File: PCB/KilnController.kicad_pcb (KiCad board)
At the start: 2 copper layers, 150 x 85 mm, 30 parts, among them J1 12V 3A PS Header, J10 Display Header, J11 Display Button Header, J12 Moisture Probe 1 Header, J13 Moisture Probe 2 Header, J2 Exhaust Fan Header, J3 Circulation Fan Header, J4 SD Card Module, J5 Exhaust Servo Header, J6 Intake Servo Header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

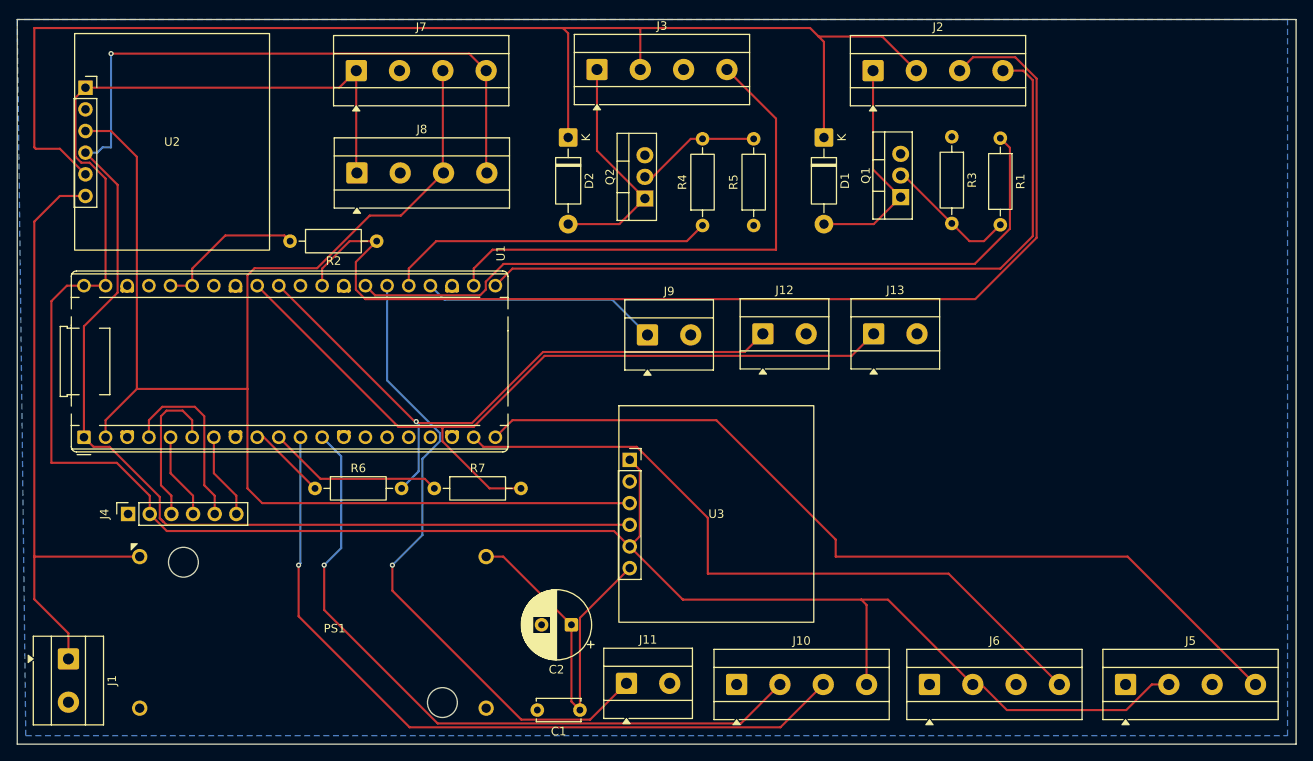
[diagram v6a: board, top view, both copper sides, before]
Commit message: Add LoRa to schematic & layout
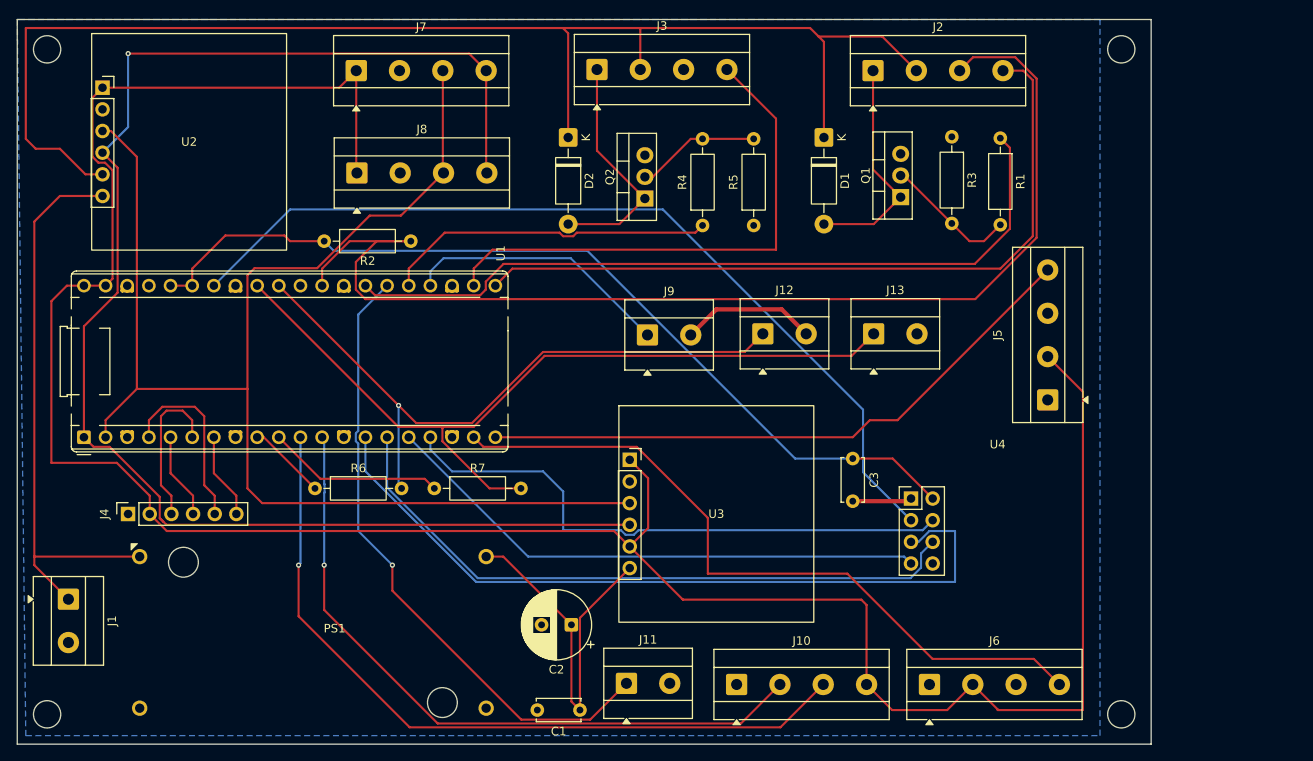
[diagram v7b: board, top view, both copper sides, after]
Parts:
- added C3: 100nF, Capacitor_THT:C_Disc_D5.0mm_W2.5mm_P5.00mm, F.Cu at (177.0, 110.5)
- added REF**: MountingHole_3.2mm_M3, MountingHole:MountingHole_3.2mm_M3, F.Cu at (82.5, 140.5)
- added REF**: MountingHole_3.2mm_M3, MountingHole:MountingHole_3.2mm_M3, F.Cu at (208.5, 62.5)
- added REF**: MountingHole_3.2mm_M3, MountingHole:MountingHole_3.2mm_M3, F.Cu at (208.5, 140.5)
- added REF**: MountingHole_3.2mm_M3, MountingHole:MountingHole_3.2mm_M3, F.Cu at (82.5, 62.5)
- added U4: Ra-02_433MHz, KilnFootprintLibrary:LoRa_Module, F.Cu at (183.8, 115.2)
- J4: footprint Connector_PinSocket_2.54mm:PinSocket_1x06_P2.54mm_Vertical -> KilnFootprintLibrary:SDCardModule
- moved J5 34.6 mm to (199.9, 103.6), turned to 90 degrees
- moved J1 7.00 mm to (85.0, 127.0)
- moved R2 4.00 mm to (115.0, 85.0)
- moved U2 2.00 mm to (89.0, 67.0)
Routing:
- net /LORA_RST: track 0.00 -> 104.9 mm
- net /LORA_SCK: track 0.00 -> 91.0 mm
- net /+3V3: track 17.9 -> 105.8 mm
- net /LORA_TX: track 0.00 -> 77.0 mm
- net /LORA_CS: track 0.00 -> 67.9 mm
- net /LORA_RX: track 0.00 -> 65.0 mm
- net /SERVO_EXHAUST: track 104.0 -> 72.9 mm
- net /+5V: track 263.4 -> 292.5 mm
- net GND: track 0.00 -> 22.9 mm
- net /FAN_EX_TACH: track 129.1 -> 137.1 mm
- net /+12V_SRC: track 72.6 -> 67.6 mm
- net /I2C0_SDA: track 178.0 -> 173.8 mm
- net /HEATER_SSR: track 27.9 -> 31.5 mm
- net /+12V: track 156.9 -> 160.3 mm
- net /I2C0_SCL: track 165.2 -> 163.2 mm
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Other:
- board size 150 x 85 mm -> 133 x 85 mm

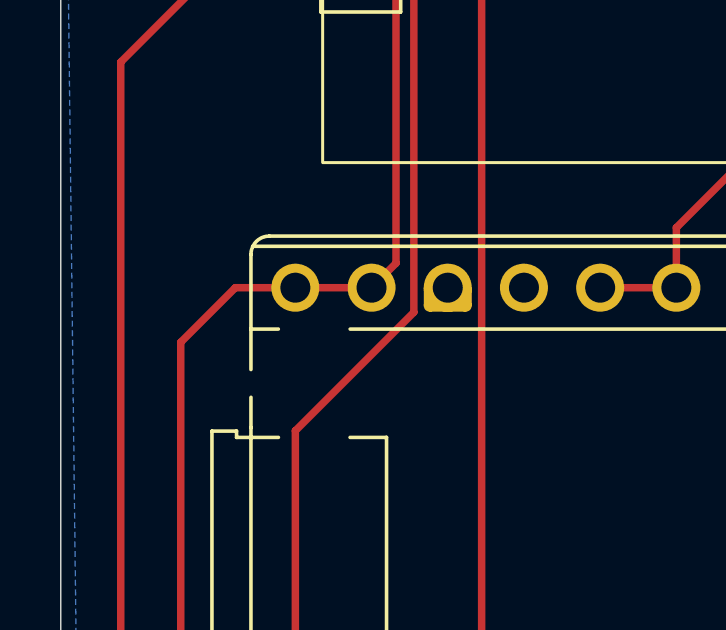
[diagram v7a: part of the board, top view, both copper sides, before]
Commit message: Remove VBUS connection
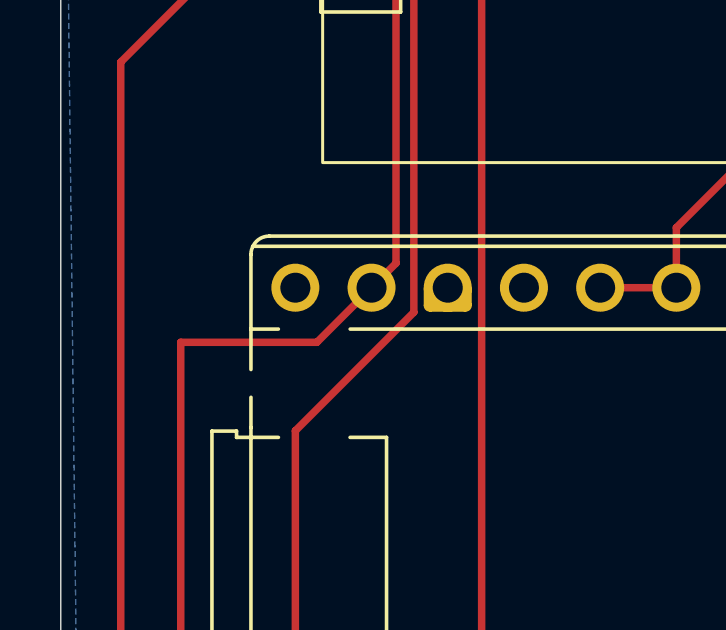
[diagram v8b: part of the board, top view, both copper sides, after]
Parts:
- J4: footprint KilnFootprintLibrary:SDCardModule -> Connector_PinSocket_2.54mm:PinSocket_1x06_P2.54mm_Vertical
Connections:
- U1 pad 40: /+5V -> unconnected-(U1-VBUS-Pad40)
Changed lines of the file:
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@@
 	(net 41 "/I2C0_SDA")
 	(net 42 "unconnected-(U4-DIO0-Pad8)")
+	(net 43 "unconnected-(U1-VBUS-Pad40)")
 	(footprint "KilnFootprintLibrary:TerminalBlock_MetzConnect_Type101_RT01604HBWC_1x04_P5.08mm_Horizontal"
 		(layer "F.Cu")
@@
 		(embedded_fonts no)
 	)
-	(footprint "KilnFootprintLibrary:SDCardModule"
+	(footprint "Connector_PinSocket_2.54mm:PinSocket_1x06_P2.54mm_Vertical"
 		(layer "F.Cu")
 		(at 92 117 90)
@@
 			(layer "F.SilkS")
 		)
-		(fp_rect
-			(start -2.54 -6.35)
-			(end 5.08 19.05)
+		(fp_line
+			(start 1.75 -1.8)
+			(end 1.75 14.45)
 			(stroke
 				(width 0.05)
-				(type default)
+				(type solid)
+			)
+			(layer "F.CrtYd")
+		)
+		(fp_line
+			(start -1.8 -1.8)
+			(end 1.75 -1.8)
+			(stroke
+				(width 0.05)
+				(type solid)
+			)
+			(layer "F.CrtYd")
+		)
+		(fp_line
+			(start 1.75 14.45)
+			(end -1.8 14.45)
+			(stroke
+				(width 0.05)
+				(type solid)
+			)
+			(layer "F.CrtYd")
+		)
+		(fp_line
+			(start -1.8 14.45)
+			(end -1.8 -1.8)
+			(stroke
+				(width 0.05)
+				(type solid)
 			)
-			(fill no)
 			(layer "F.CrtYd")
 		)
@@
 		)
 		(fp_text user "${REFERENCE}"
-			(at 0 6.35 0)
+			(at 0 6.35 180)
 			(layer "F.Fab")
 			(effects
@@
 			(layers "*.Cu" "*.Mask")
 			(remove_unused_layers no)
-			(net 2 "/+5V")
+			(net 43 "unconnected-(U1-VBUS-Pad40)")
 			(pinfunction "VBUS")
-			(pintype "power_in")
+			(pintype "power_in+no_connect")
 		)
 		(zone
@@
 	)
 	(segment
-		(start 89.36 90.22)
-		(end 86.82 90.22)
-		(width 0.25)
-		(layer "F.Cu")
-		(net 2)
-	)
-	(segment
 		(start 153 118.65)
 		(end 153 112.81)
@@
 	)
 	(segment
-		(start 84.82 90.22)
-		(end 86.82 90.22)
-		(width 0.25)
-		(layer "F.Cu")
-		(net 2)
-	)
-	(segment
 		(start 94.54 117)
 		(end 94.54 114.86)
@@
 	)
 	(segment
+		(start 83 92.04)
+		(end 87.54 92.04)
+		(width 0.25)
+		(layer "F.Cu")
+		(net 2)
+	)
+	(segment
 		(start 87.825 68.175)
 		(end 89 67)
@@
 	)
 	(segment
-		(start 83 92.04)
-		(end 84.82 90.22)
-		(width 0.25)
-		(layer "F.Cu")
-		(net 2)
-	)
-	(segment
 		(start 178.62 137)
 		(end 181.62 140)
@@
 		(width 0.25)
 		(layer "F.Cu")
+		(net 2)
+	)
+	(segment
+		(start 87.54 92.04)
+		(end 89.36 90.22)
+		(width 0.25)
+		(layer "F.Cu")
